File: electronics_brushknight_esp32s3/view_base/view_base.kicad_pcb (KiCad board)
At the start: 4 copper layers, 81.2 x 81.2 mm, 250 parts, among them J1 BLDC, J2 USB_C_Receptacle_USB2.0, J3 LCD, J4 A, J5 B, J6 LCD - FPC, J7 Conn_01x04_Socket, J8 Conn_01x04_Socket, J9 Conn_01x04_Socket, Q1 MMBT4403, Q2 BSS138, Q3 BSS138, U1 MT6701-CT, U10 ESP32-S3-WROOM-1-N8R8, U2 USBLC6-2SC6, U3 VL53L0CXV0DH_1, U4 HX711, U5 TMC6300, U6 LP5907MFX-2.8, U7 SN74LV1T34DBV, U8 VEML7700, U9 TS1117BCW33_RPG

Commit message: run DRC
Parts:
- added R28: 10k, cleaned footprints:R_0603_1608Metric, F.Cu at (84.2, 136.7)
- added SW1: RST, smd_clean:SW_SPST_PTS810, B.Cu at (79.8, 132.2)
- added SW2: Boot, smd_clean:SW_SPST_PTS810, B.Cu at (75.8, 132.2)
- moved Z5 83.7 mm to (100.0, 100.0)
- moved TP12 2.00 mm to (83.8, 138.2)
- moved TP13 2.00 mm to (79.8, 138.2)
- moved TP14 2.00 mm to (75.8, 138.2)
- moved TP15 2.00 mm to (67.8, 138.2)
- moved TP16 2.00 mm to (71.8, 138.2)
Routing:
- net GND: track 32.1 -> 67.6 mm, vias 40 -> 42
- net +5V: track 43.7 -> 69.6 mm, vias 70 -> 77
- net /ESP32_BOOT: track 27.7 -> 48.1 mm
- net /ESP32_EN: track 11.0 -> 18.8 mm, vias 3 -> 2
- net /USB_SERIAL_TXO: track 14.0 -> 16.0 mm
- net /USB_SERIAL_RXI: track 9.54 -> 11.5 mm
- net /LED_DATA_5V: track 31.8 -> 29.8 mm
- net /STRAIN_E+: track 123.2 -> 121.7 mm
- net +3V3: vias 27 -> 24
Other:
- board text added: "RST"

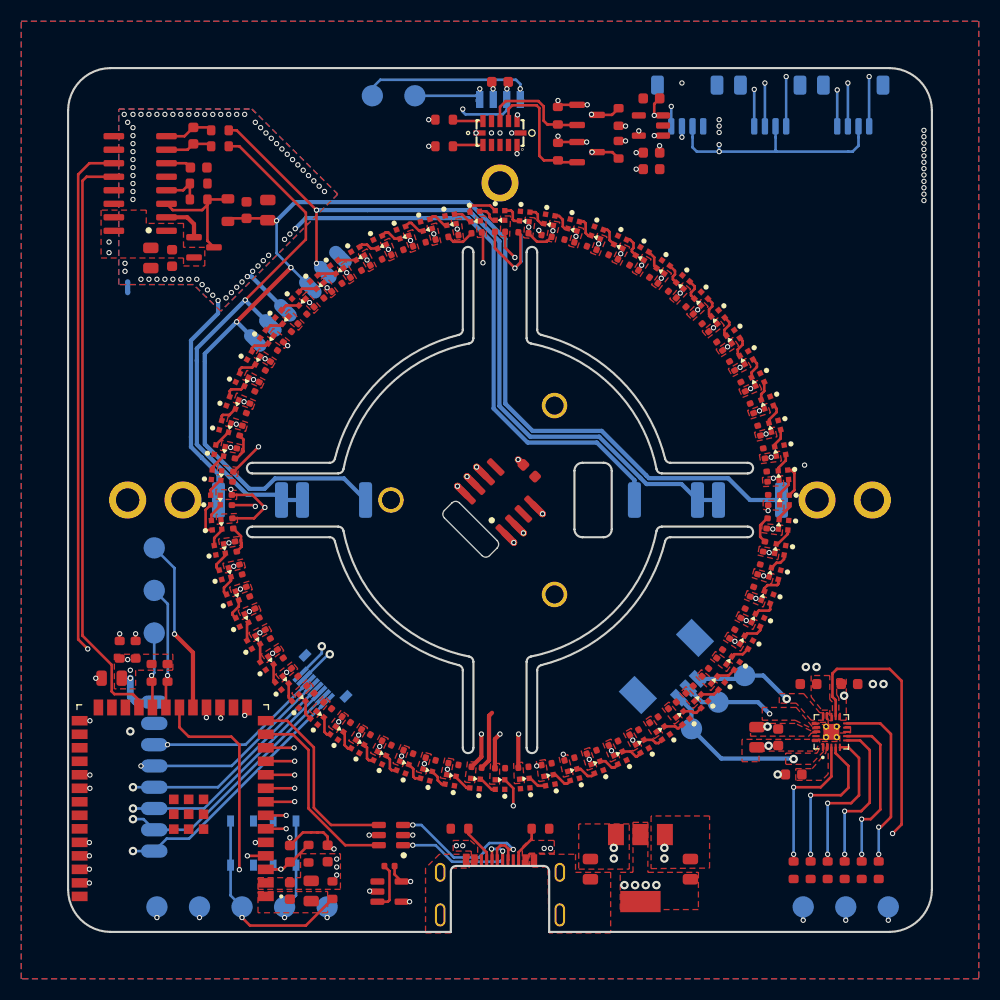
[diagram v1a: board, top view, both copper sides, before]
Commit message: working on a panel, run DRC for base pcb
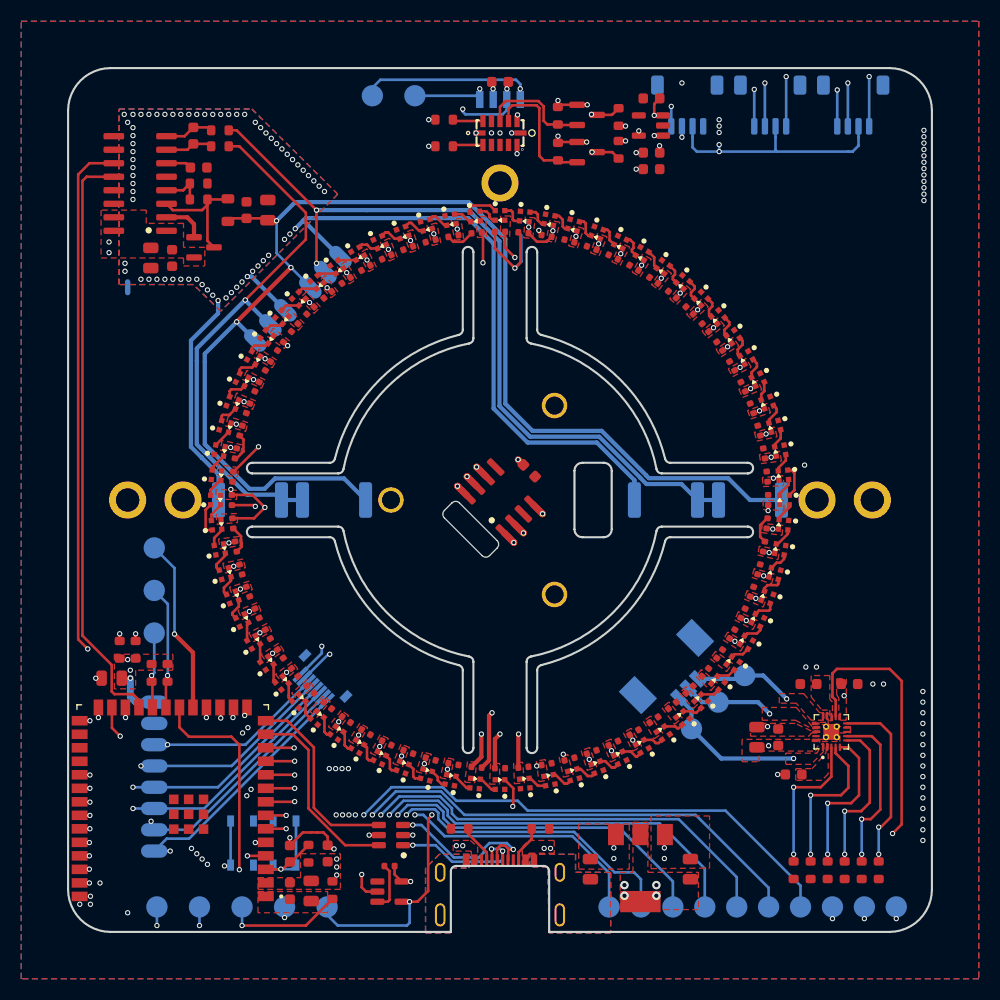
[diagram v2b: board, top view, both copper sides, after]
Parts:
- removed Z5: dummy_keepouts, view_custom:ViewKeepouts3d
- added TP17: IO40, cleaned footprints:TestPoint_Pad_D2.0mm_ValueSilk, B.Cu at (116.2, 138.2)
- added TP18: IO41, cleaned footprints:TestPoint_Pad_D2.0mm_ValueSilk, B.Cu at (113.2, 138.2)
- added TP19: IO42, cleaned footprints:TestPoint_Pad_D2.0mm_ValueSilk, B.Cu at (110.2, 138.2)
- added TP20: IO45, cleaned footprints:TestPoint_Pad_D2.0mm_ValueSilk, B.Cu at (119.2, 138.2)
- added TP21: IO46, cleaned footprints:TestPoint_Pad_D2.0mm_ValueSilk, B.Cu at (128.2, 138.2)
- added TP22: IO47, cleaned footprints:TestPoint_Pad_D2.0mm_ValueSilk, B.Cu at (125.2, 138.2)
- added TP23: IO48, cleaned footprints:TestPoint_Pad_D2.0mm_ValueSilk, B.Cu at (122.2, 138.2)
- moved TP1 2.75 mm to (131.2, 138.2)
- moved TP3 1.75 mm to (134.2, 138.2)
- moved TP2 0.75 mm to (137.2, 138.2)
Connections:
- U10 pad 16: unconnected-(U10-IO46-Pad16) -> Net-(U10-IO46)
- U10 pad 24: unconnected-(U10-IO47-Pad24) -> Net-(U10-IO47)
- U10 pad 25: unconnected-(U10-IO48-Pad25) -> Net-(U10-IO48)
- U10 pad 26: unconnected-(U10-IO45-Pad26) -> Net-(U10-IO45)
- U10 pad 33: unconnected-(U10-IO40-Pad33) -> Net-(U10-IO40)
- U10 pad 34: unconnected-(U10-IO41-Pad34) -> Net-(U10-IO41)
- U10 pad 35: unconnected-(U10-IO42-Pad35) -> Net-(U10-IO42)
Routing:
- net Net-(U10-IO46): track 0.00 -> 104.6 mm, vias 0 -> 2
- net Net-(U10-IO47): track 0.00 -> 93.0 mm, vias 0 -> 2
- net Net-(U10-IO48): track 0.00 -> 91.2 mm, vias 0 -> 2
- net Net-(U10-IO45): track 0.00 -> 87.4 mm, vias 0 -> 2
- net Net-(U10-IO40): track 0.00 -> 76.1 mm, vias 0 -> 2
- net Net-(U10-IO41): track 0.00 -> 72.2 mm, vias 0 -> 2
- net Net-(U10-IO42): track 0.00 -> 68.0 mm, vias 0 -> 2
- net /ESP32_BOOT: track 48.1 -> 56.1 mm, vias 2 -> 5
- net GNDA: track 79.5 -> 84.1 mm
- net /LED_DATA_3V3: track 34.7 -> 38.7 mm
- net /LCD_CMD: track 29.7 -> 32.7 mm
- net /ESP32_EN: track 18.8 -> 16.0 mm
- net /USB_SERIAL_TXO: track 16.0 -> 18.7 mm
- net /USB_SERIAL_RXI: track 11.5 -> 14.0 mm
- net /LED_DATA_5V: track 29.8 -> 32.0 mm
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
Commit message: minor changes for PCBs order
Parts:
- added REF**: seedlabs_smartknob, seedlabs:seedlabs_smartknob, F.Cu at (128.5, 68.0)
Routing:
- net +5V: track 70.2 -> 79.1 mm, vias 77 -> 78
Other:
- board text added: "01"
- board text added: "DEVKIT"
- board text added: "SUBJECT"
- board text added: "v0.1"
- board text removed: "SmartKnob DevKit"
- board text removed: "esp32s3"

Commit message: Updated ibom for base pcb
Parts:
- D10, D11, D12, D13, D14, D15, D16, D17, D18, D19, D20, D21, D22, D23, D24, D25, D26, D27, D28, D29, D30, D31, D32, D33, D34, D35, D36, D37, D38, D39, D40, D41, D42, D43, D44, D45, D46, D47, D48, D49, D50, D51, D52, D53, D54, D55, D56, D57, D58, D59, D60, D61, D62, D63, D64, D65, D66, D67, D68, D69, D70, D71, D72, D73, D74, D75, D76, D77, D78, D79, D80, D9: value SK6812 -> SK6805
